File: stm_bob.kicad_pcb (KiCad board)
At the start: 4 copper layers, 142 x 141 mm, 113 parts, among them J1 Conn_01x02, J10_GPIO1 Conn_01x02, J11_SPI1 Conn_01x03, J2 Conn_01x04_Pin, J3 Conn_01x04_Pin, J4 Conn_01x02_Pin, J5 Conn_01x04_Pin, J6 Conn_01x04_Pin, J7 Conn_01x02_Pin, J9_GPIO1 Conn_01x02, J9_GPIO2 Conn_01x02, Q1 NPN, U1 LTV-817S, U10 LTV-817S, U2 LTV-817S, U3 LTV-817S, U3V3+1 R-78E3.3-1.0, U4 LTV-817S, U5 LTV-817S, U5V+1 R-78E5.0-1.0, U6 LTV-817S, U7 LTV-817S, U8 LM358, U9 LM358

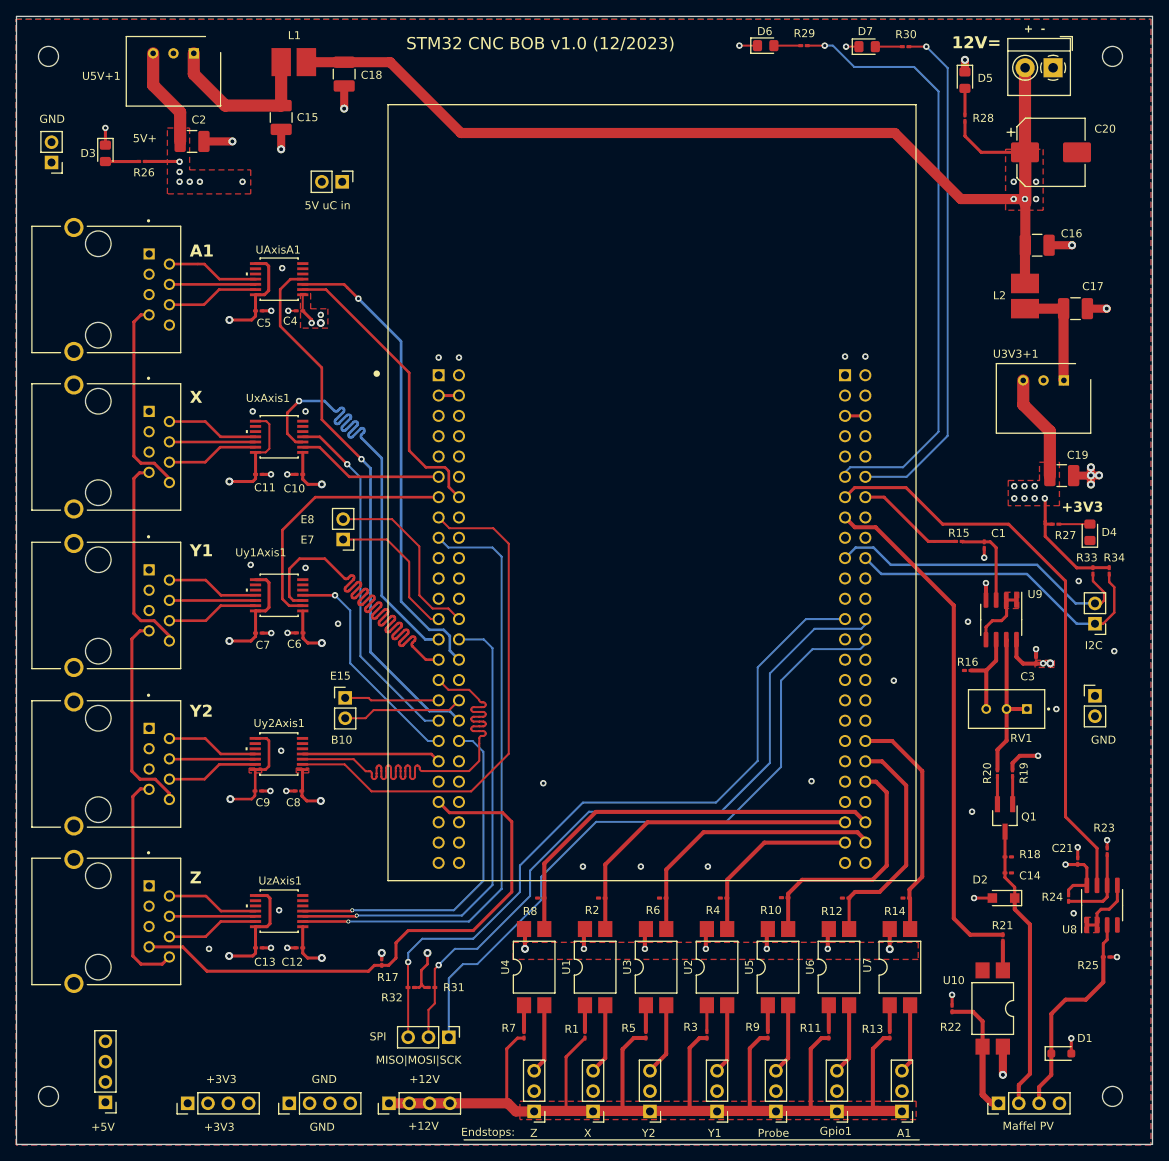
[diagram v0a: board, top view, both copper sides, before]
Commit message: Version 1.1 - reworked all smd's to 0603
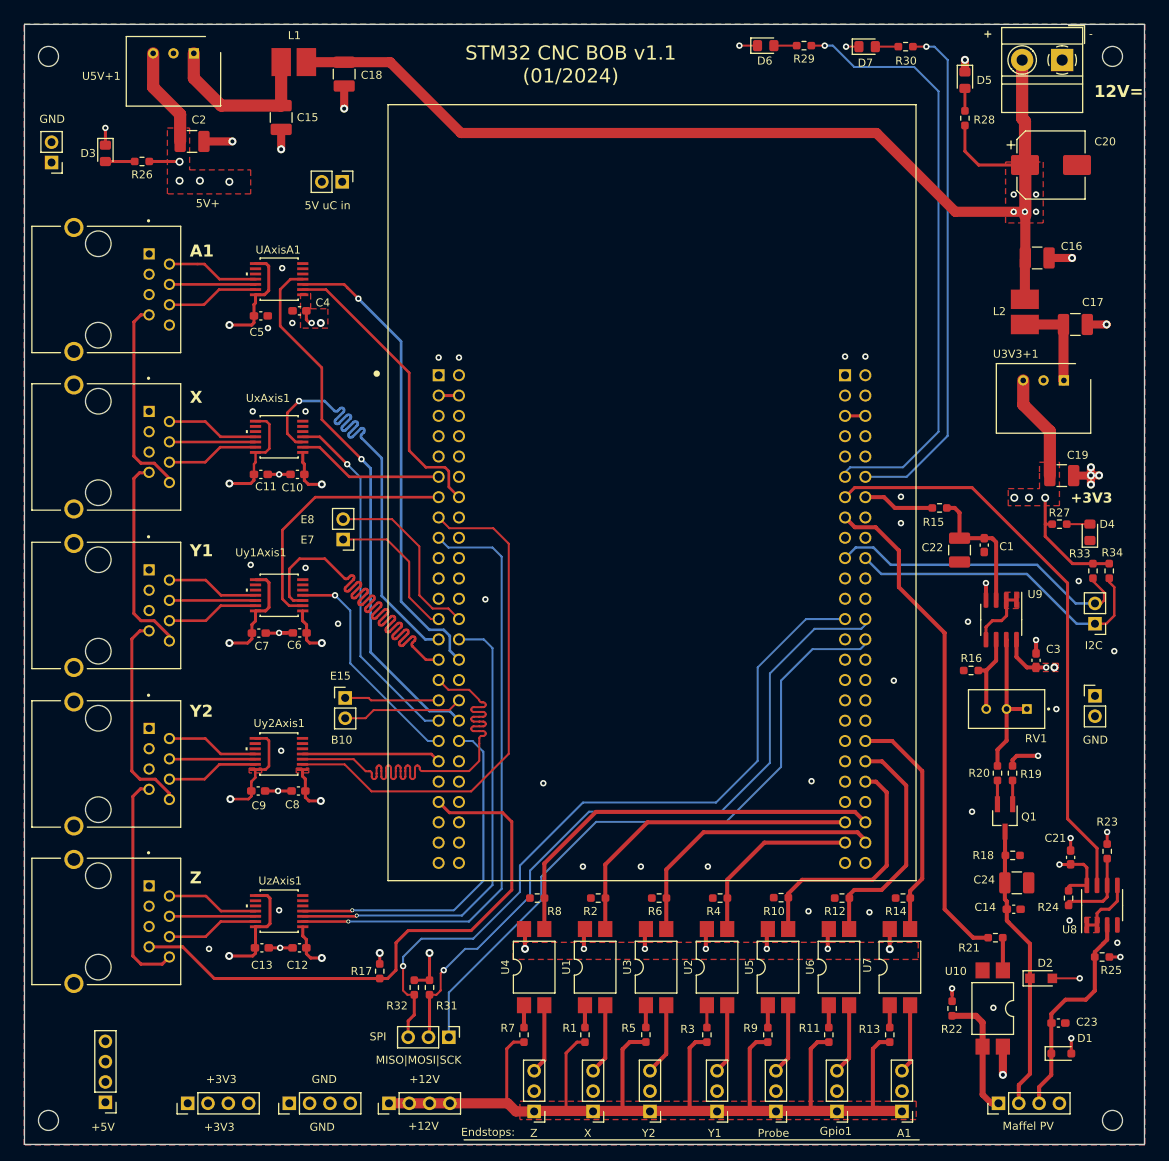
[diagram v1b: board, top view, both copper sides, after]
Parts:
- added C22: 10uF, Inductor_SMD:L_1210_3225Metric_Pad1.42x2.65mm_HandSolder, F.Cu at (137.9, 96.7)
- added C23: C, Capacitor_SMD:C_0603_1608Metric_Pad1.08x0.95mm_HandSolder, F.Cu at (150.2, 155.8)
- added C24: 10uF, Inductor_SMD:L_1210_3225Metric_Pad1.42x2.65mm_HandSolder, F.Cu at (145.0, 138.3)
- C1: value C -> 100n; footprint Capacitor_SMD:C_0201_0603Metric_Pad0.64x0.40mm_HandSolder -> Capacitor_SMD:C_0603_1608Metric_Pad1.08x0.95mm_HandSolder
- C10, C11, C12, C13, C14, C21, C3, C4, C5, C6, C7, C8, C9: footprint Capacitor_SMD:C_0201_0603Metric_Pad0.64x0.40mm_HandSolder -> Capacitor_SMD:C_0603_1608Metric_Pad1.08x0.95mm_HandSolder
- J1: footprint TerminalBlock_4Ucon:TerminalBlock_4Ucon_1x02_P3.50mm_Horizontal -> TerminalBlock_MetzConnect:TerminalBlock_MetzConnect_Type011_RT05502HBWC_1x02_P5.00mm_Horizontal
- R1, R10, R11, R12, R13, R14, R15, R16, R17, R18, R19, R2, R20, R21, R22, R23, R24, R25, R26, R27, R28, R29, R3, R30, R31, R32, R33, R34, R4, R5, R6, R7, R8, R9: footprint Resistor_SMD:R_0201_0603Metric_Pad0.64x0.40mm_HandSolder -> Resistor_SMD:R_0603_1608Metric_Pad0.98x0.95mm_HandSolder
- moved D2 11.1 mm to (148.1, 150.2), turned to 0 degrees
- moved R15 4.84 mm to (135.4, 91.4)
- moved C14 4.59 mm to (144.7, 141.6)
- moved H2 3.00 mm to (24.0, 168.0)
- moved H3 3.00 mm to (157.0, 168.0)
- moved C17 1.98 mm to (152.4, 68.5)
- moved L2 1.98 mm to (146.1, 66.9)
- moved C20 1.59 mm to (149.3, 48.6)
- moved C16 1.59 mm to (147.6, 60.2)
- moved J1 1.49 mm to (150.7, 35.5)
- moved R17 1.17 mm to (65.4, 149.4)
- moved C21 1.00 mm to (151.8, 135.1)
- moved R21 0.93 mm to (142.4, 145.2), turned to 0 degrees
- moved C5 0.68 mm to (50.5, 67.4)
- moved R18 0.59 mm to (144.5, 134.9)
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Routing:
- net Net-(U9A-+): track 11.1 -> 17.0 mm
- net GND: track 51.1 -> 56.6 mm, vias 57 -> 59
- net SpindlePWM: track 13.6 -> 8.92 mm
- net +3V3: track 312.5 -> 308.6 mm, vias 24 -> 19
- net Net-(U3V3+1-+VIN): track 13.8 -> 11.9 mm
- net +12V: track 488.6 -> 490.5 mm
- net SPI_MISO: track 91.2 -> 93.0 mm
- net SpindleEnable: track 64.2 -> 62.6 mm
- net error_stepper: track 70.8 -> 72.3 mm
- net SPI_SCK: track 85.4 -> 84.3 mm
- net Net-(D4-A): track 3.89 -> 2.90 mm
- net Net-(U9B--): track 11.1 -> 10.2 mm
- net Net-(Q1-B): track 3.47 -> 2.96 mm
- net Net-(R5-Pad2): track 3.28 -> 2.77 mm
- net LED1: track 75.7 -> 75.2 mm
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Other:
- board size 142 x 141 mm -> 140 x 140 mm
- board text added: "+"
- board text added: "-"
- board text added: "STM32 CNC BOB v1.1 (01/2024)"
- board text removed: "+ -"
- board text removed: "STM32 CNC BOB v1.0 (12/2023)"

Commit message: Updating 12V on/off with FET now; Laser connectors added
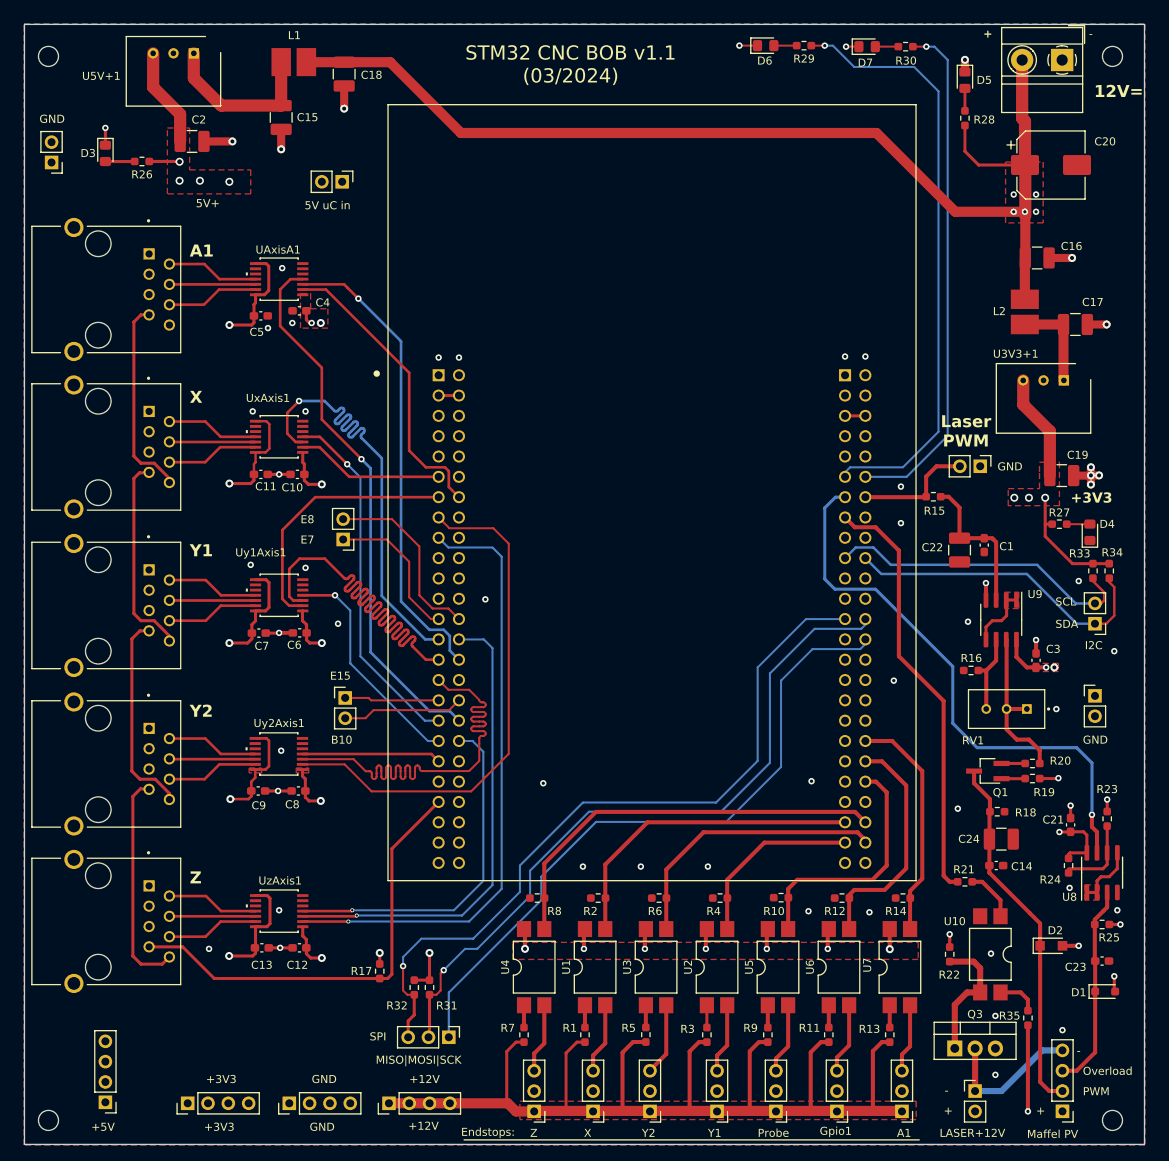
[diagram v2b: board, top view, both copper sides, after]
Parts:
- added JLaser12V1: Conn_01x02_Pin, Connector_PinHeader_2.54mm:PinHeader_1x02_P2.54mm_Vertical, F.Cu at (139.8, 164.3)
- added JLaserPWM1: Conn_01x02_Pin, Connector_PinHeader_2.54mm:PinHeader_1x02_P2.54mm_Vertical, F.Cu at (140.5, 86.2)
- added Q3: IRF3205, Package_TO_SOT_THT:TO-220-3_Vertical, F.Cu at (137.3, 159.0)
- added R35: 1k, Resistor_SMD:R_0603_1608Metric_Pad0.98x0.95mm_HandSolder, F.Cu at (146.4, 155.2)
- R22: value 4k7 -> 2k
- moved D1 9.49 mm to (156.1, 151.9)
- moved C23 9.48 mm to (155.7, 148.1)
- moved JPvMaffel1 8.06 mm to (150.7, 166.9), turned to 180 degrees
- moved R21 7.96 mm to (138.6, 138.2)
- moved R22 6.78 mm to (136.7, 147.2)
- moved U10 6.78 mm to (141.7, 147.2)
- moved Q1 6.24 mm to (141.4, 124.3), turned to 180 degrees
- moved C14 5.88 mm to (142.5, 136.1)
- moved R18 5.79 mm to (142.6, 129.4)
- moved C24 5.79 mm to (143.1, 132.8)
- moved R20 4.54 mm to (147.0, 123.4), turned to 0 degrees
- moved D2 4.26 mm to (149.4, 146.2)
- moved R23 4.06 mm to (156.3, 130.3)
- moved R25 4.06 mm to (155.7, 143.5)
- moved U8 4.06 mm to (155.7, 137.0)
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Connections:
- JPvMaffel1 pad 1: Net-(JPvMaffel1-Pin_1) -> +12V
- JPvMaffel1 pad 4: GND -> Net-(JLaser12V1-Pin_1)
- R22 pad 1: Net-(JPvMaffel1-Pin_1) -> Net-(Q3-G)
- U10 pad 3: Net-(JPvMaffel1-Pin_1) -> Net-(Q3-G)
- U10 pad 4: +12V -> Net-(R35-Pad2)
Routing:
- net Net-(JLaser12V1-Pin_1): track 0.00 -> 18.4 mm
- net Net-(Q3-G): track 0.00 -> 16.5 mm
- net error_stepper: track 72.3 -> 56.2 mm
- net Net-(JPvMaffel1-Pin_1): track 15.6 -> 0.00 mm
- net Upv_maffel: track 35.9 -> 45.4 mm
- net SpindleEnable: track 62.6 -> 53.5 mm
- net SpindlePWM: track 8.92 -> 14.9 mm
- net Net-(R35-Pad2): track 0.00 -> 5.18 mm
- net +12V: track 490.5 -> 494.4 mm
- net Net-(R21-Pad2): track 4.10 -> 6.49 mm
- net SpindleOverload: track 72.6 -> 70.6 mm, vias 0 -> 1
- net Net-(R20-Pad2): track 18.8 -> 20.6 mm
- net Net-(U9A-+): track 17.0 -> 18.8 mm
- net Uo_overload: track 27.3 -> 25.7 mm
- net GND: track 56.6 -> 55.2 mm, vias 59 -> 62
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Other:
- board text added: "LASER+12V"
- board text added: "Laser PWM"
- board text added: "Overload"
- board text added: "PWM"
- board text added: "SCL"
- board text added: "SDA"
- board text added: "STM32 CNC BOB v1.1 (03/2024)"
- board text removed: "STM32 CNC BOB v1.1 (01/2024)"

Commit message: Make GND vias larger, some cleanups
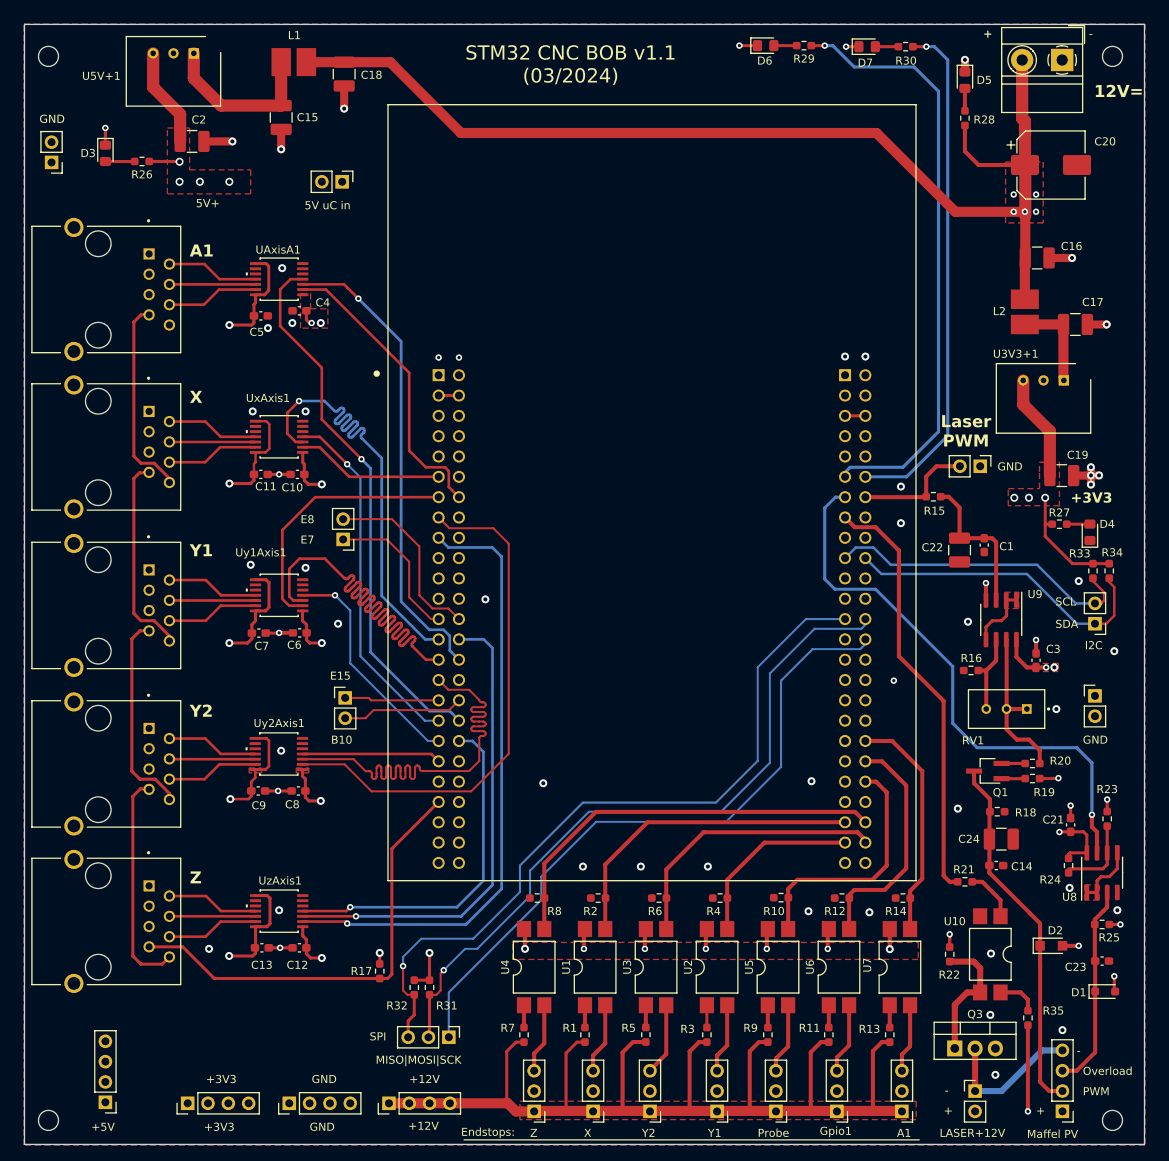
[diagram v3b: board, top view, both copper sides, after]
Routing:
- net +5V: track 226.2 -> 222.5 mm

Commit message: Adding Coolant and Mist; some GPIOs added
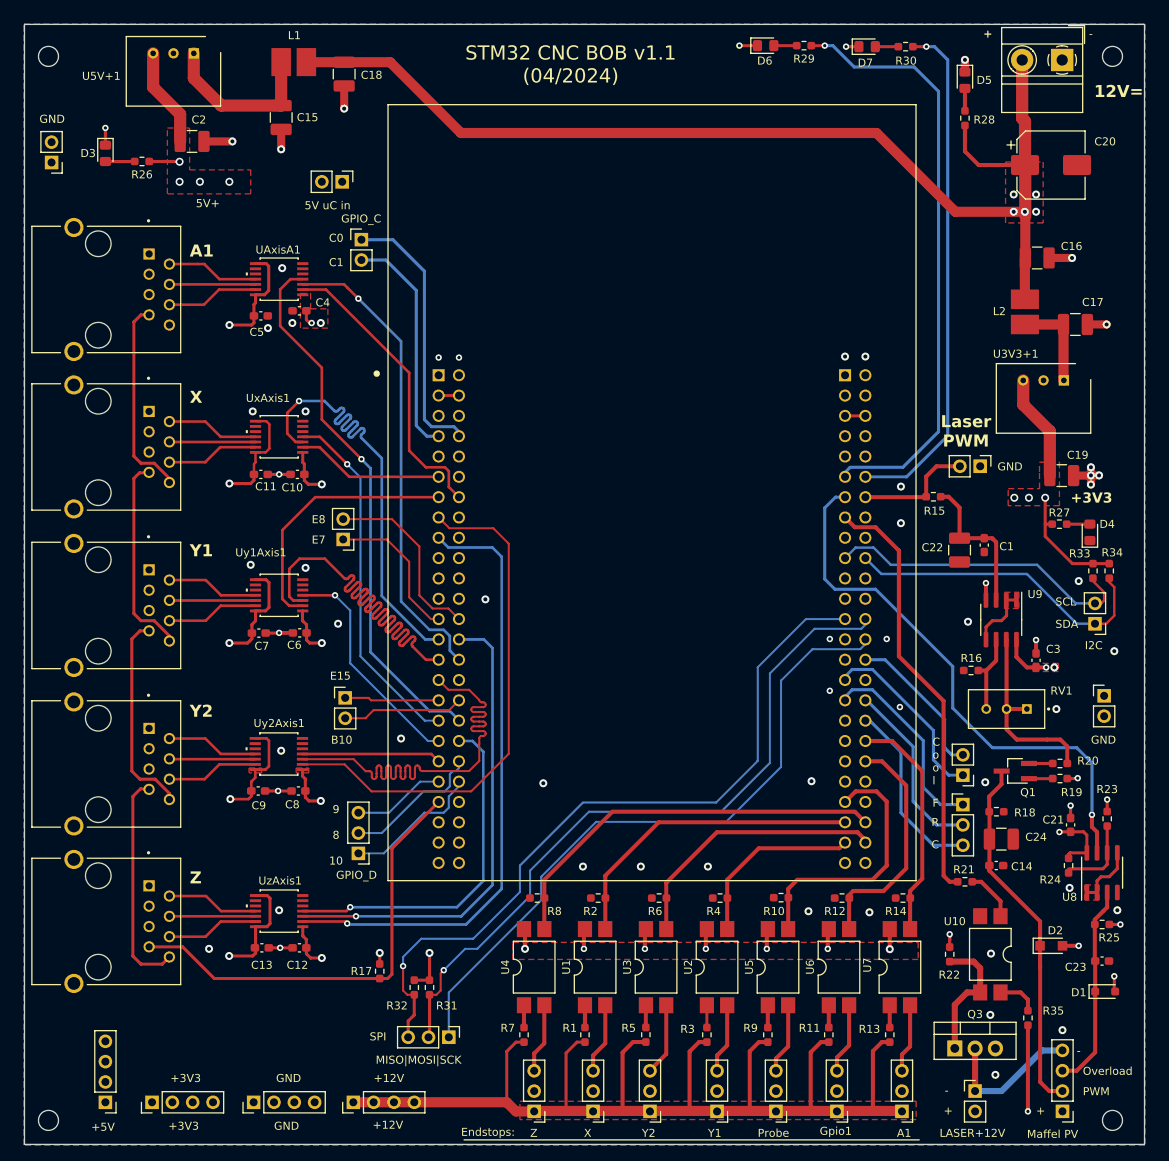
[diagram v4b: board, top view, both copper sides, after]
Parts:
- added J11_GPIO1: Conn_01x03, Connector_PinHeader_2.54mm:PinHeader_1x03_P2.54mm_Vertical, F.Cu at (62.7, 134.6)
- added J11_SPI2: Conn_01x03, Connector_PinHeader_2.54mm:PinHeader_1x03_P2.54mm_Vertical, F.Cu at (138.3, 128.5)
- added J9_GPIO3: Conn_01x02, Connector_PinHeader_2.54mm:PinHeader_1x02_P2.54mm_Vertical, F.Cu at (63.1, 57.9)
- added J9_GPIO4: Conn_01x02, Connector_PinHeader_2.54mm:PinHeader_1x02_P2.54mm_Vertical, F.Cu at (138.3, 124.8)
- moved J5 4.46 mm to (62.1, 165.7)
- moved J3 4.46 mm to (36.9, 165.7)
- moved J6 4.46 mm to (49.6, 165.7)
- moved Q1 3.44 mm to (144.8, 124.3)
- moved R19 3.44 mm to (150.4, 125.3)
- moved R20 3.44 mm to (150.4, 123.4)
- moved J4 1.14 mm to (156.0, 114.9)
- moved R18 0.10 mm to (142.5, 129.4)
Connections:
- TB1 pad P1_40: unconnected-(TB1-PD8-PadP1_40) -> GPIO_PD08
- TB1 pad P1_41: unconnected-(TB1-PD9-PadP1_41) -> GPIO_PD09
- TB1 pad P1_42: unconnected-(TB1-PD10-PadP1_42) -> GPIO_PD10
- TB1 pad P1_7: unconnected-(TB1-PC1-PadP1_7) -> GPIO_PC1
- TB1 pad P1_8: unconnected-(TB1-PC0-PadP1_8) -> GPIO_PC0
- TB1 pad P2_30: unconnected-(TB1-PD6-PadP2_30) -> coolant_mist
- TB1 pad P2_31: unconnected-(TB1-PD3-PadP2_31) -> coolant_flood
- TB1 pad P2_42: Probe -> unconnected-(TB1-PA13-PadP2_42)
- TB1 pad P2_43: unconnected-(TB1-PA8-PadP2_43) -> Probe
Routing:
- net GPIO_PC0: track 0.00 -> 33.6 mm
- net GPIO_PC1: track 0.00 -> 28.7 mm
- net FeedHold: track 0.00 -> 24.9 mm
- net coolant_flood: track 0.00 -> 23.2 mm
- net CycleStart: track 0.00 -> 23.1 mm
- net Reset: track 0.00 -> 22.7 mm
- net coolant_mist: track 0.00 -> 19.2 mm
- net GPIO_PD08: track 0.00 -> 17.7 mm
- net GPIO_PD10: track 0.00 -> 17.4 mm
- net GPIO_PD09: track 0.00 -> 11.6 mm
- net +12V: track 494.4 -> 500.0 mm
- net Net-(R20-Pad2): track 20.6 -> 24.4 mm
- net Probe: track 30.9 -> 32.8 mm
- net +3V3: track 310.0 -> 311.7 mm
- net limitZ: track 51.5 -> 50.4 mm
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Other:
- board text added: "9 8 10"
- board text added: "C"
- board text added: "C o o l"
- board text added: "C0"
- board text added: "C1"
- board text added: "F"
- board text added: "GPIO_C"
- board text added: "GPIO_D"
- board text added: "R"
- board text added: "STM32 CNC BOB v1.1 (04/2024)"
- board text removed: "STM32 CNC BOB v1.1 (03/2024)"

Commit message: Updating for version 1.1
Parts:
- added H5: MountingHole_Pad, MountingHole:MountingHole_3mm_Pad, F.Cu at (25.0, 159.8)
- R29, R30: value R -> 510
- moved J9_GPIO1 0.13 mm to (61.1, 115.1)
- moved R27 0.13 mm to (150.5, 93.5)
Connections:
- TB1 pad P1_12: unconnected-(TB1-PA0-WKUP-PadP1_12) -> dirY2
- TB1 pad P1_14: dirA -> dirZ
- TB1 pad P1_15: dirY2 -> unconnected-(TB1-PA5-PadP1_15)
- TB1 pad P1_17: dirZ -> dirA
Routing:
- net GND: track 55.2 -> 63.2 mm, vias 66 -> 78
- net dirA: track 37.1 -> 44.5 mm, vias 0 -> 1
- net GPIO_PC0: track 33.6 -> 39.0 mm
- net dirY2: track 65.5 -> 67.8 mm
- net dirZ: track 77.2 -> 79.2 mm
- net stepA: track 59.1 -> 60.4 mm
